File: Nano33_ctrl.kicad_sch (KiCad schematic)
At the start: 53 parts, among them J1 To Protec_Brd, J12 Conn_01x02, J15 To Display, J17 Conn_01x02, J18 To Protec_Brd encoder, J19 To P.A., J4 Power_In, J5 Conn_01x02, J6 Conn_01x02, U12 Arduino-NANO-33, U2 LM1117S-5.0, U3 LM1117S-3.3, U4 74HCT04, U5 TPIC6595, U6 TPIC6595, U7 TPIC6595, U8 24FC1025-I_SN, U9 24FC1025-I_SN

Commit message: more passive component layout, new silkscreen
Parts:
- removed D55: 1SS355VM, Diode_SMD:D_1210_3225Metric_Pad1.42x2.65mm_HandSolder, symbol Diode:1SS355VM
- C68: footprint Capacitor_Tantalum_SMD:CP_EIA-6032-28_Kemet-C_Pad2.25x2.35mm_HandSolder -> Capacitor_SMD:C_0805_2012Metric_Pad1.18x1.45mm_HandSolder
- U9: footprint Package_DIP:DIP-8_W8.89mm_SMDSocket_LongPads -> Package_DIP:DIP-8_W7.62mm_SMDSocket_SmallPads
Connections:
- net at C101.1, J12.1 (Pin_1), J4.1 (Pin_1)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: now also F2.1
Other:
- note removed: "changer package régulateurs TO323 probablement"
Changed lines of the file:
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@@
-    (stroke (width 0) (type default))
-  )
-  (wire (pts (xy 43.18 131.445) (xy 45.72 131.445))
     (stroke (width 0) (type default))
   )
@@
     (stroke (width 0) (type default))
   )
-  (wire (pts (xy 31.75 131.445) (xy 35.56 131.445))
+  (wire (pts (xy 31.75 131.445) (xy 45.72 131.445))
     (stroke (width 0) (type default))
   )
@@
   (text "STAND\nALONE\n\n" (at 26.035 119.38 0)
     (effects (font (size 1.27 1.27)) (justify left bottom))
-  )
-  (text "changer package régulateurs\nTO323 probablement\n" (at 78.74 125.095 0)
-    (effects (font (size 2 2) (thickness 0.4) bold) (justify left bottom))
   )
   (text "To Antenna switch" (at 257.175 59.69 0)
@@
       (effects (font (size 1.27 1.27)))
     )
-    (property "Footprint" "Package_DIP:DIP-8_W8.89mm_SMDSocket_LongPads" (at 102.235 10.795 0)
+    (property "Footprint" "Package_DIP:DIP-8_W7.62mm_SMDSocket_SmallPads" (at 102.235 10.795 0)
       (effects (font (size 1.27 1.27)) (justify left) hide)
     )
@@
     )
   )
-  (symbol (lib_id "Diode:1SS355VM") (at 39.37 131.445 180) (unit 1)
-    (in_bom yes) (on_board yes) (dnp no) (fields_autoplaced)
-    (property "Reference" "D55" (at 39.37 127.1651 0)
-      (effects (font (size 1.27 1.27)))
-    )
-    (property "Value" "1SS355VM" (at 39.37 129.0861 0)
-      (effects (font (size 1.27 1.27)))
-    )
-    (property "Footprint" "Diode_SMD:D_1210_3225Metric_Pad1.42x2.65mm_HandSolder" (at 39.37 127 0)
-      (effects (font (size 1.27 1.27)) hide)
-    )
-    (property "Datasheet" "https://fscdn.rohm.com/en/products/databook/datasheet/discrete/diode/switching/1ss355vmte-17-e.pdf" (at 39.37 131.445 0)
-      (effects (font (size 1.27 1.27)) hide)
-    )
-    (property "Sim.Device" "D" (at 39.37 131.445 0)
-      (effects (font (size 1.27 1.27)) hide)
-    )
-    (property "Sim.Pins" "1=K 2=A" (at 39.37 131.445 0)
-      (effects (font (size 1.27 1.27)) hide)
-    )
-    (pin "1")
-    (pin "2")
-    (instances
-      (project "K_Aries"
-        (path "/4d56c8f7-829b-457e-80cb-74e9f55628bb/7e6cc0ee-07cc-4c77-b42a-9ca9fe554781"
-          (reference "D55") (unit 1)
-        )
-      )
-    )
-  )
   (symbol (lib_id "Connector_Generic:Conn_02x05_Odd_Even") (at 25.4 159.385 0) (unit 1)
     (in_bom yes) (on_board yes) (dnp no) (fields_autoplaced)
@@
       (effects (font (size 1.27 1.27)) (justify left))
     )
-    (property "Footprint" "Capacitor_Tantalum_SMD:CP_EIA-6032-28_Kemet-C_Pad2.25x2.35mm_HandSolder" (at 73.025 133.985 0)
-      (effects (font (size 1.27 1.27)) hide)
-    )
+    (property "Footprint" "Capacitor_SMD:C_0805_2012Metric_Pad1.18x1.45mm_HandSolder" (at 73.025 133.985 0)
+      (effects (font (size 1.27 1.27)) hide)
+    )

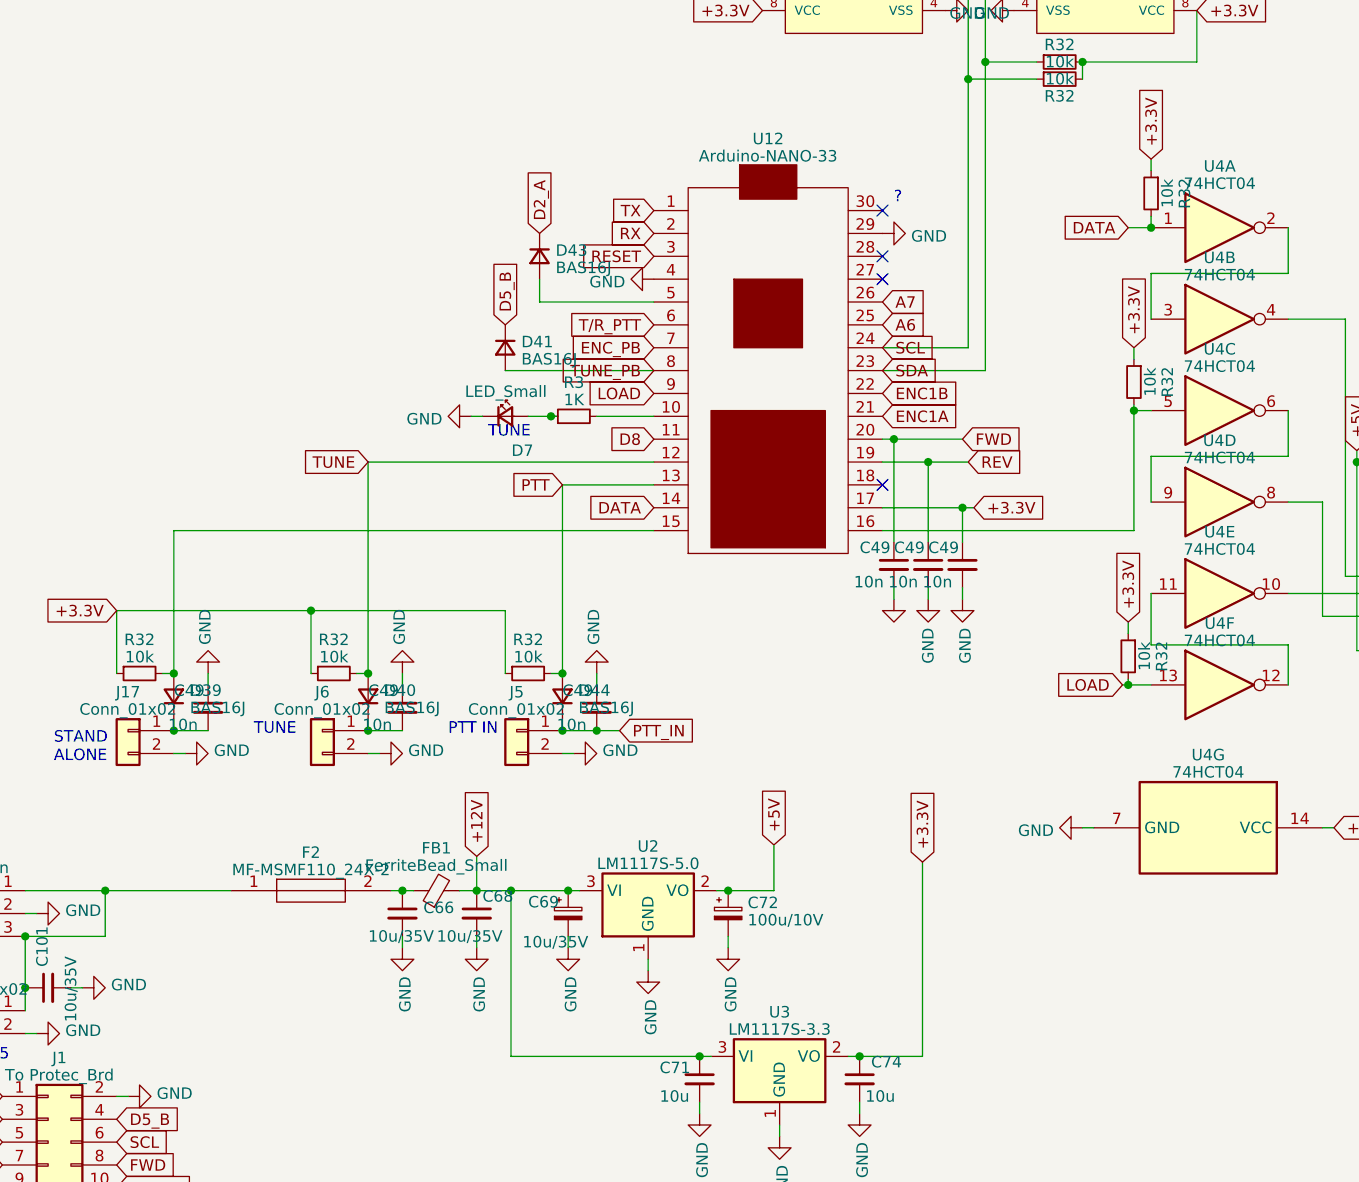
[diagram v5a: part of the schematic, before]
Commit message: all components are placed
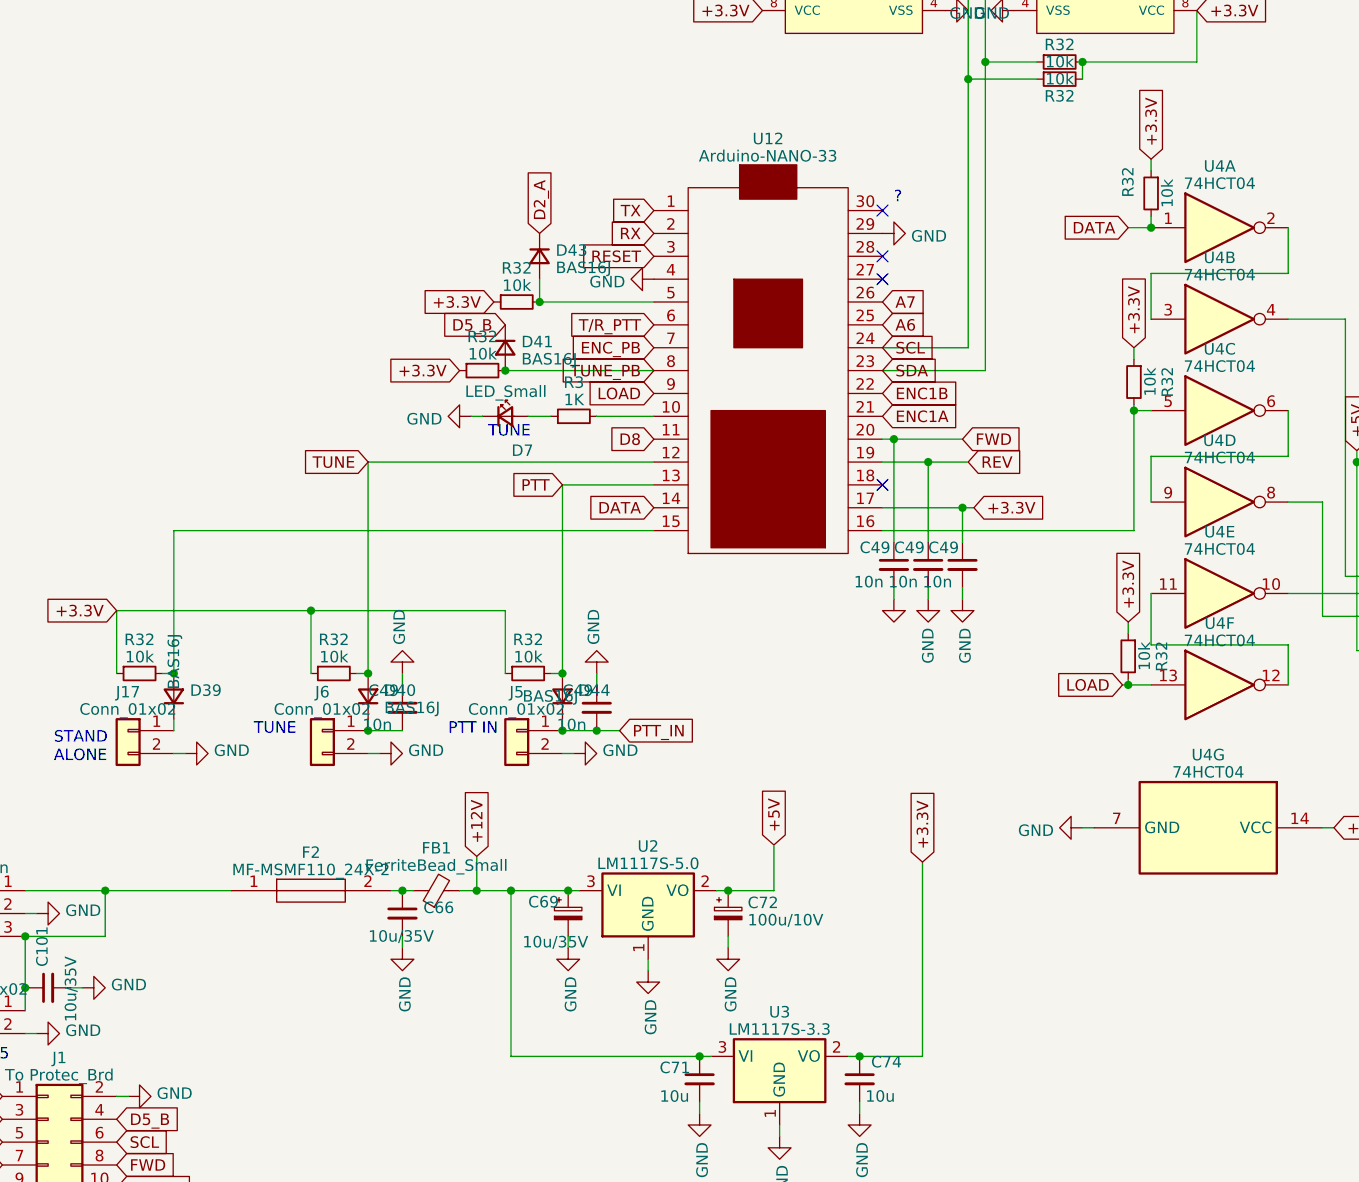
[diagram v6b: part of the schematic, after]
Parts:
- removed C49: 10n, Capacitor_SMD:C_0805_2012Metric_Pad1.18x1.45mm_HandSolder, symbol Device:C_Small
- removed C68: 10u/35V, Capacitor_SMD:C_0805_2012Metric_Pad1.18x1.45mm_HandSolder, symbol Device:C_Small
- added R32 (x2): 10k, Resistor_SMD:R_0805_2012Metric_Pad1.20x1.40mm_HandSolder, symbol Device:R_Small
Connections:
- net +3.3V: now also R32.1, R32.1
- net TUNE_PB: now also R32.2
- net at D43.2 (A), U12.5: now also R32.2

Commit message: intermediate git, more traces to come
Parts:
- added C49 (x3): 10n, Capacitor_SMD:C_0805_2012Metric_Pad1.18x1.45mm_HandSolder, symbol Device:C_Small
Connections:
- net +5V: now also C49.1
- net GND: now also C49.1, C49.1, C49.2
- net PTT: now also C49.2
- net TUNE: now also C49.2
- net CAP1 renamed Cap1
- net CAP2 renamed Cap2
- net CAP3 renamed Cap3
- net CAP4 renamed Cap4
- net CAP5 renamed Cap5
- net CAP6 renamed Cap6
- net CAP7 renamed Cap7
- net CAP8 renamed Cap8
- net IND1 renamed Ind1
- net IND2 renamed Ind2
- net IND3 renamed Ind3
- net IND4 renamed Ind4
- net IND5 renamed Ind5
- net IND6 renamed Ind6
- net IND7 renamed Ind7
- net IND8 renamed Ind8
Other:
- note added: "C74 et C75 à ajouter"

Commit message: minor schematic mods
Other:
- note removed: "C74 et C75 à ajouter"
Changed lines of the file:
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@@
     (effects (font (size 1.27 1.27)) (justify left bottom))
-  )
-  (text "C74 et C75 à ajouter" (at 36.195 43.815 0)
-    (effects (font (size 3 3) (thickness 0.6) bold) (justify left bottom))
   )
   (text "To transformer section" (at 178.435 59.055 0)
